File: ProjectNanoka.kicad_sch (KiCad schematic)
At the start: 32 parts, among them K1 2-1462038-1, P1 ST_20A, Q1 2SC1815, Q2 2SC1815, U1 TLV70033DDCR, U2 NC7WZ16P6X, U3 PS1440P02BT

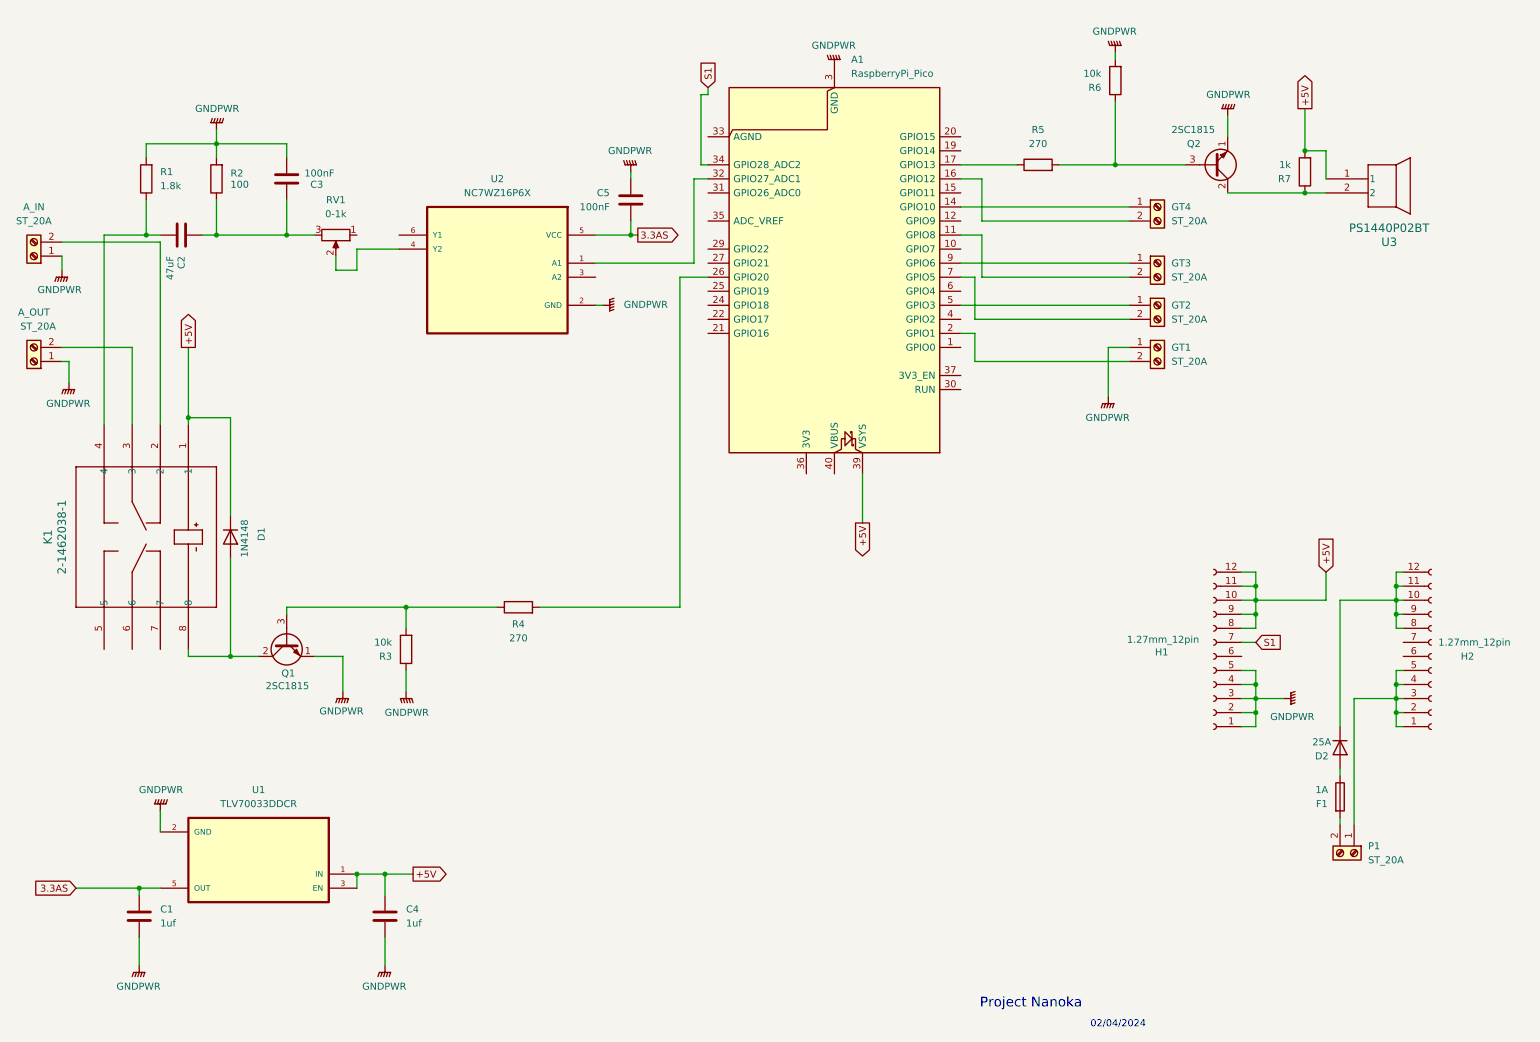
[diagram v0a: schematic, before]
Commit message: Fix issues found in v1
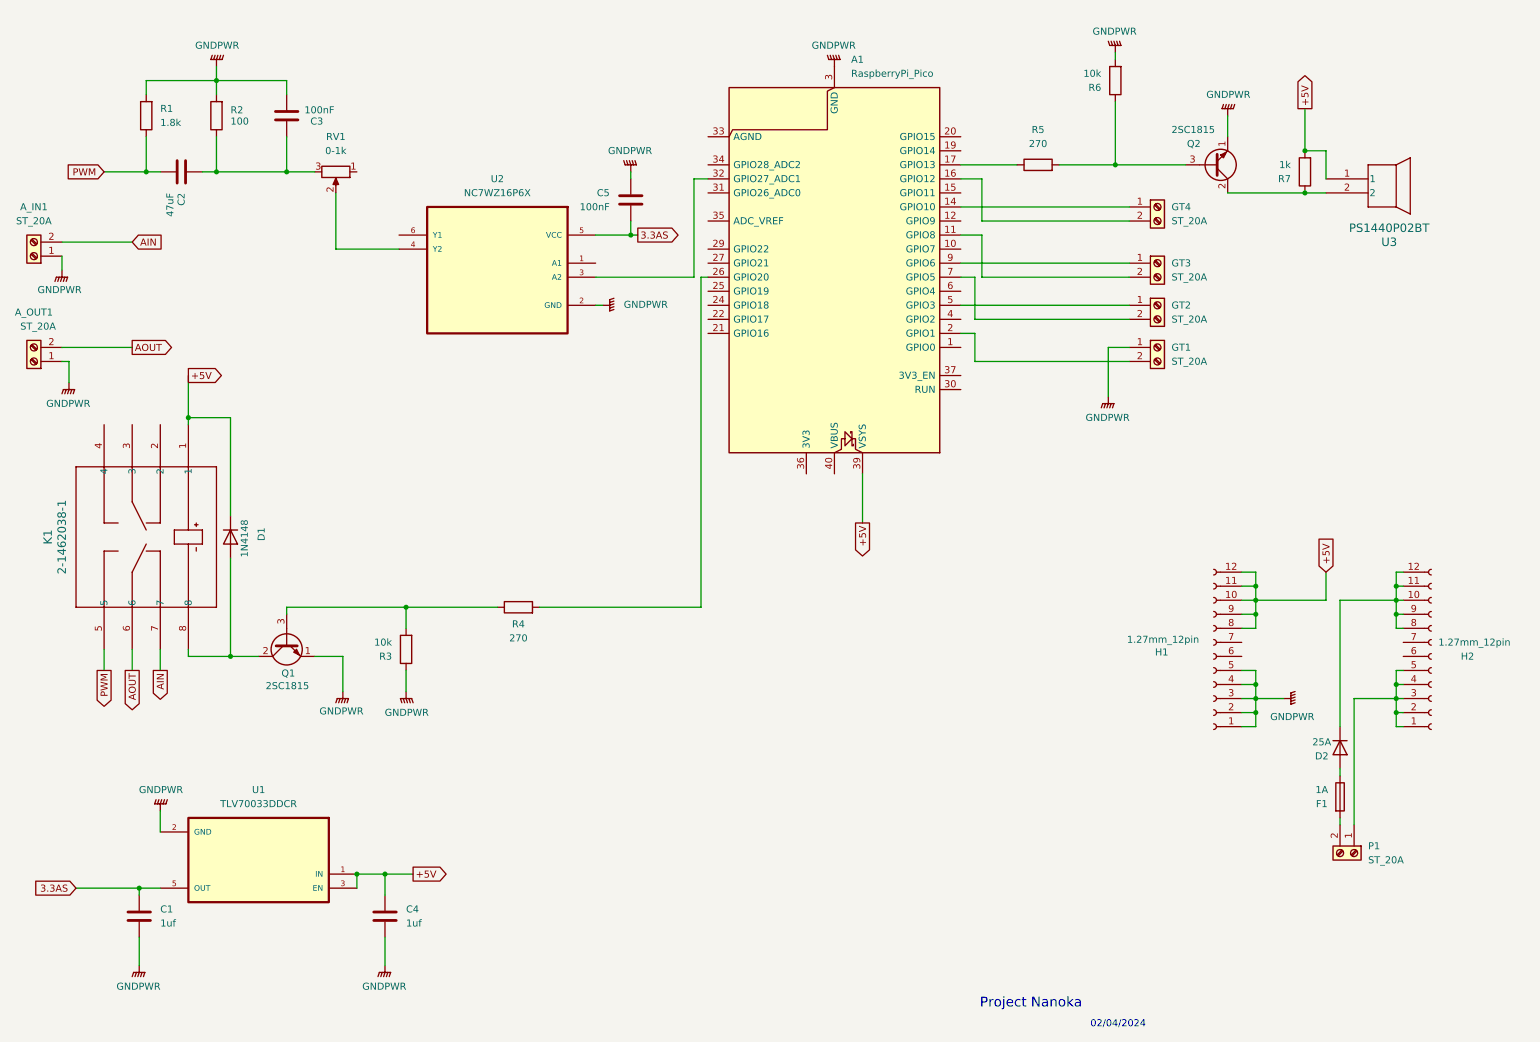
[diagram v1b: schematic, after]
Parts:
- K1: footprint Custom:RELAY8_THTNRW_TEC -> Custom:RELAY8-TH_NON-LATCH_1-COIL
- renumbered A_IN to A_IN1, A_OUT to A_OUT1
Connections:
- net at K1.3: no longer A_OUT1.2 (Pin_2)
- net PWM: now reaches C2.2, R1.1
- net PWM: now also K1.5; no longer K1.4
- net at A1.32 (GPIO27_ADC1): now also U2.3 (A2); no longer U2.1 (A1)
- net at K1.2: no longer A_IN1.2 (Pin_2)
- net AOUT: now reaches K1.6
- net AOUT: now also A_OUT1.2 (Pin_2)
- net AIN: now reaches K1.7
- net AIN: now also A_IN1.2 (Pin_2)
- net S1: no longer names the net of H1.7 (Pin_7)
- net S1: no longer A1.34 (GPIO28_ADC2)
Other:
- moved on the sheet: C2, C3, R1, R2, RV1

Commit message: Make improvements to board
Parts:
- A1: footprint Custom:RPi_Pico_SMD_TH -> Footprints:RPi_Pico_SMD_TH; symbol MCU_Module:RaspberryPi_Pico -> Symbols:RaspberryPi_Pico
- A_IN1, A_OUT1, GT1, GT2, GT3, GT4, P1: footprint Custom:CONN_1935161_PXC -> Footprints:CONN_1935161_PXC; symbol Connector:Screw_Terminal_01x02 -> Symbols:Screw_Terminal_01x02
- C1, C4: footprint Custom:CAP_C330C_MR_X7R_KEM -> Footprints:CAP_C330C_MR_X7R_KEM; symbol Device:C -> Symbols:C
- C2: footprint Custom:CAP_UUQ_5X5P4_NCH -> Footprints:CAP_UUQ_5X5P4_NCH; symbol Device:C -> Symbols:C
- C3, C5: footprint Custom:CAP_C320_KEM -> Footprints:CAP_C320_KEM; symbol Device:C -> Symbols:C
- D1: footprint Diode_THT:D_DO-35_SOD27_P7.62mm_Horizontal -> Footprints:D_DO-35_SOD27_P7.62mm_Horizontal; symbol Diode:1N4148 -> Symbols:1N4148
- D2: footprint Custom:P33_D5.4x7.5 -> Footprints:P33_D5.4x7.5; symbol Device:D -> Symbols:D
- F1: footprint Custom:20x300_FUSE_HOLDER_0PTF0078P_LTF -> Footprints:20x300_FUSE_HOLDER_0PTF0078P_LTF; symbol Device:Fuse -> Symbols:Fuse
- H1, H2: footprint Custom:PinHeader_1x12_P1.27mm_Vertical_Modded -> Footprints:PinHeader_1x12_P1.27mm_Vertical_Modded; symbol Connector:Conn_01x12_Socket -> Symbols:Conn_01x12_Socket
- K1: footprint Custom:RELAY8-TH_NON-LATCH_1-COIL -> Footprints:RELAY8-TH_NON-LATCH_1-COIL; symbol audio relay 2:2-1462038-1 -> Symbols:2-1462038-1
- Q1, Q2: footprint Package_TO_SOT_THT:TO-92_Inline -> Footprints:TO-92_Inline; symbol Transistor_BJT:2SC1815 -> Symbols:2SC1815
- R1, R2: footprint Custom:STA_CF14_STP -> Footprints:STA_CF14_STP; symbol Device:R -> Symbols:R
- R3, R4, R5, R6, R7: footprint Custom:STA_RNF14_STP -> Footprints:STA_RNF14_STP; symbol Device:R -> Symbols:R
- RV1: footprint Custom:TRIM_3310Y-101-102L -> Footprints:TRIM_3310Y-101-102L; symbol Device:R_Potentiometer -> Symbols:R_Potentiometer
- U1: footprint Custom:SOT95P280X110-5N -> Footprints:SOT95P280X110-5N; symbol TLV70033DDCR:TLV70033DDCR -> Symbols:TLV70033DDCR
- U2: footprint Custom:SOT65P210X110-6N -> Footprints:SOT65P210X110-6N; symbol NC7WZ16P6X:NC7WZ16P6X -> Symbols:NC7WZ16P6X
- U3: footprint Custom:PS1440P02BT_TDK -> Footprints:PS1440P02BT_TDK; symbol piezo:PS1440P02BT -> Symbols:PS1440P02BT

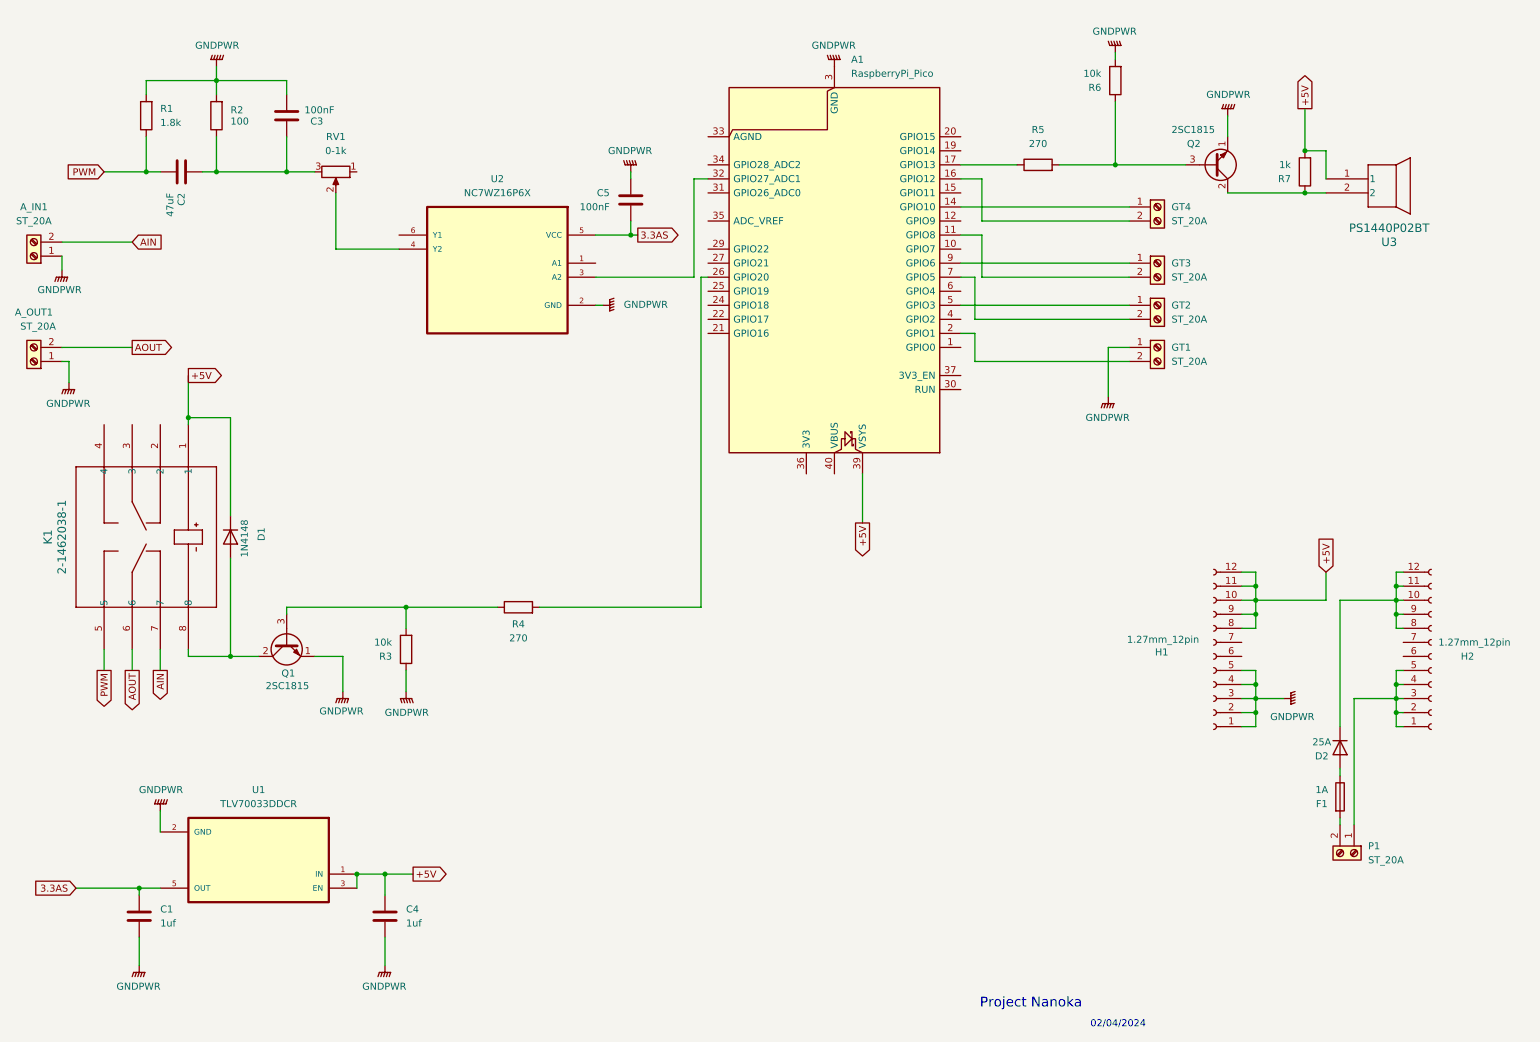
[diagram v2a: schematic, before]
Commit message: Replaced 2SC1815 with 2N3904BU
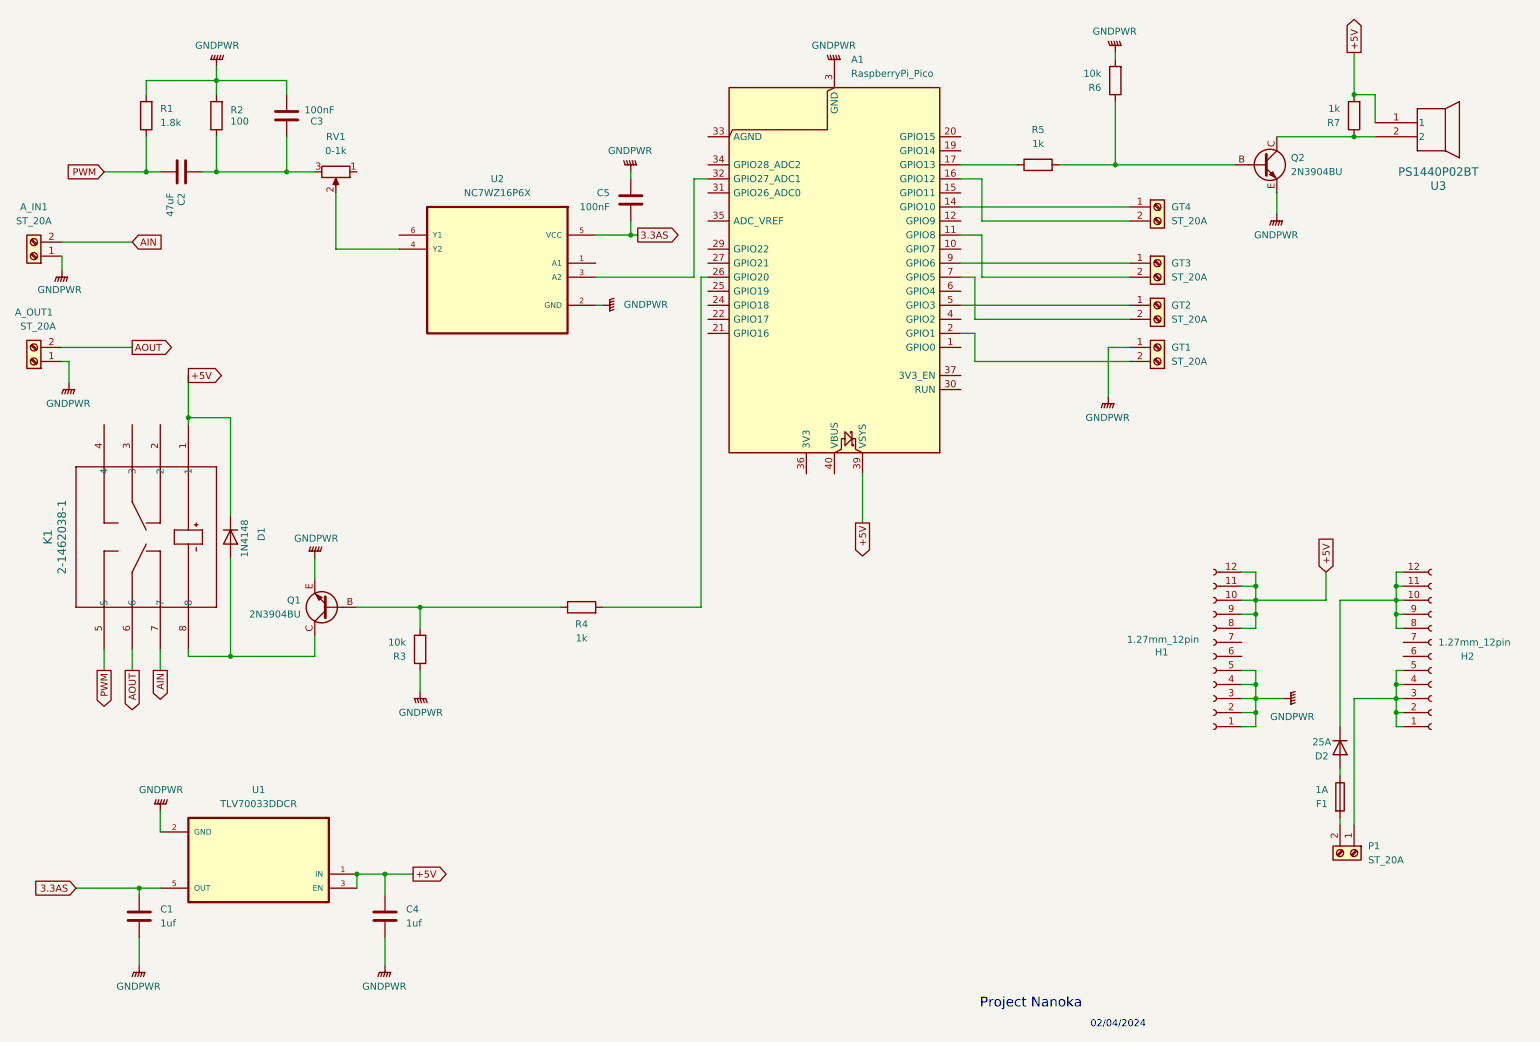
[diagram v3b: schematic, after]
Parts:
- removed Q1, Q2: 2SC1815, Footprints:TO-92_Inline, symbol Symbols:2SC1815
- added Q1, Q2: 2N3904BU, Footprints:2N3904BU, symbol Symbols:2N3904BU
- R4, R5: value 270 -> 1k
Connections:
- net GNDPWR: now also Q1.E, Q2.E
- net at R5.2, R6.1: now also Q2.B
- net at R7.1, U3.2: now also Q2.C
- net at R3.2, R4.1: now also Q1.B
- net at D1.2 (A), K1.8: now also Q1.C
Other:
- moved on the sheet: R3, R4, R7, U3

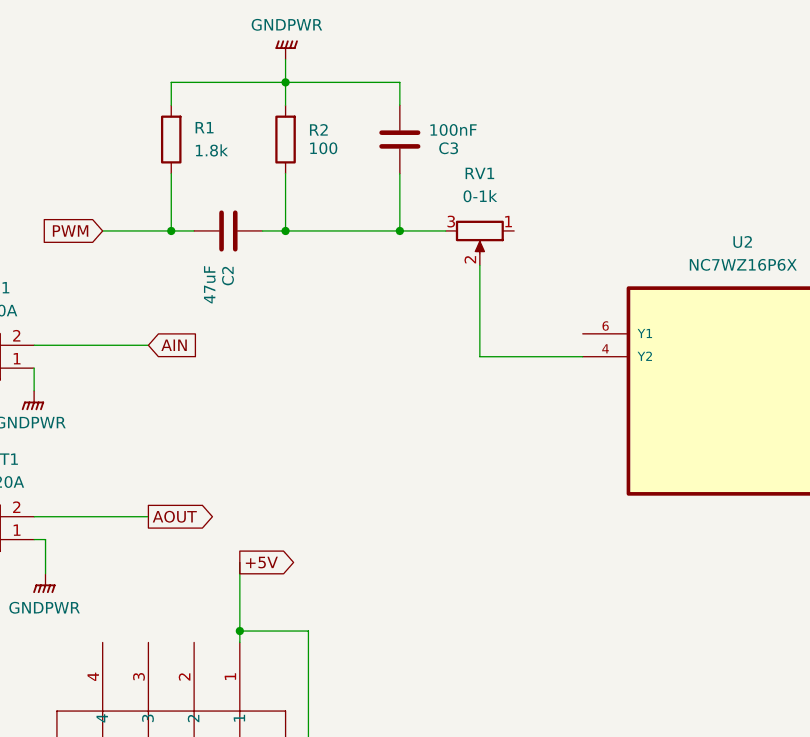
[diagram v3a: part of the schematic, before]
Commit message: Replaced RV1 with a 220ohm resistor
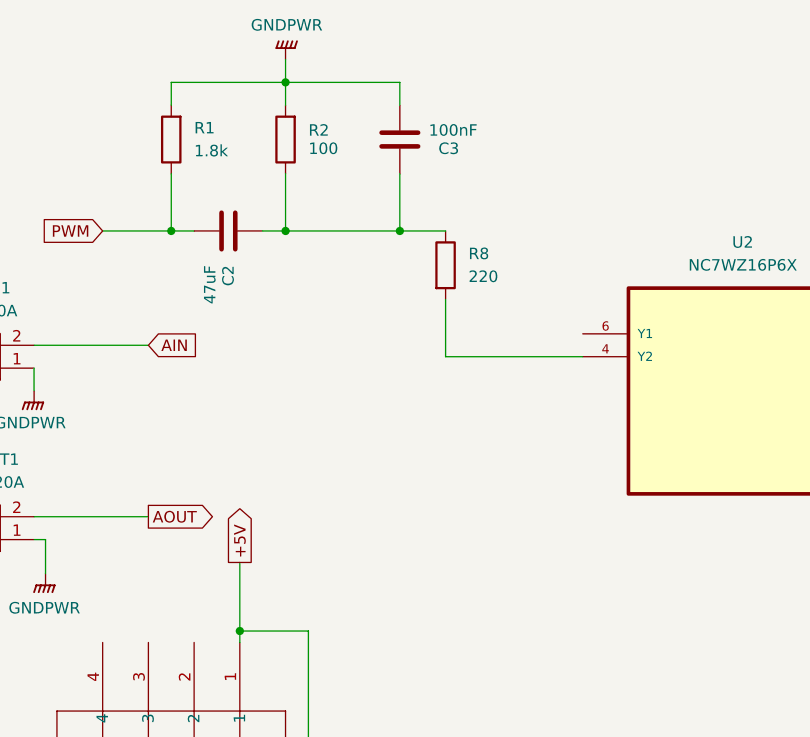
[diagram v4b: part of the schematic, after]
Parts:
- removed RV1: 0-1k, Footprints:TRIM_3310Y-101-102L, symbol Symbols:R_Potentiometer
- added R8: 220, Footprints:STA_RNMF14_STP, symbol Symbols:R
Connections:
- net at U2.4 (Y2): now also R8.2
- net at C2.1, C3.1, R2.1: now also R8.1
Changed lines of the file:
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@@
 	(wire
 		(pts
-			(xy 71.12 53.34) (xy 82.55 53.34)
+			(xy 67.31 53.34) (xy 82.55 53.34)
 		)
 		(stroke
@@
 	(wire
 		(pts
-			(xy 71.12 43.18) (xy 71.12 53.34)
+			(xy 67.31 46.99) (xy 67.31 53.34)
 		)
 		(stroke
@@
 	(global_label "+5V"
 		(shape output)
-		(at 44.45 76.2 0)
+		(at 44.45 76.2 90)
 		(fields_autoplaced yes)
 		(effects
@@
 		)
 		(property "Intersheetrefs" "${INTERSHEET_REFS}"
-			(at 51.3057 76.2 0)
+			(at 44.45 69.3443 90)
 			(effects
 				(font
@@
 				(path "/b82cdc01-ed0f-4544-82ee-3986c13336e7"
 					(reference "#PWR03")
-					(unit 1)
-				)
-			)
-		)
-	)
-	(symbol
-		(lib_id "Symbols:R_Potentiometer")
-		(at 71.12 39.37 270)
-		(unit 1)
-		(exclude_from_sim no)
-		(in_bom yes)
-		(on_board yes)
-		(dnp no)
-		(property "Reference" "RV1"
-			(at 71.12 33.02 90)
-			(effects
-				(font
-					(size 1.27 1.27)
-				)
-			)
-		)
-		(property "Value" "0-1k"
-			(at 71.12 35.56 90)
-			(effects
-				(font
-					(size 1.27 1.27)
-				)
-			)
-		)
-		(property "Footprint" "Footprints:TRIM_3310Y-101-102L"
-			(at 71.12 39.37 0)
-			(effects
-				(font
-					(size 1.27 1.27)
-				)
-				(hide yes)
-			)
-		)
-		(property "Datasheet" "~"
-			(at 71.12 39.37 0)
-			(effects
-				(font
-					(size 1.27 1.27)
-				)
-				(hide yes)
-			)
-		)
-		(property "Description" "Potentiometer"
-			(at 71.12 39.37 0)
-			(effects
-				(font
-					(size 1.27 1.27)
-				)
-				(hide yes)
-			)
-		)
-		(pin "1"
-		)
-		(pin "2"
-		)
-		(pin "3"
-		)
-		(instances
-			(project ""
-				(path "/b82cdc01-ed0f-4544-82ee-3986c13336e7"
-					(reference "RV1")
 					(unit 1)
 				)
@@
 					(unit 1)
 				)
+			)
+		)
+	)
+	(symbol
+		(lib_id "Symbols:R")
+		(at 67.31 43.18 0)
+		(unit 1)
+		(exclude_from_sim no)
+		(in_bom yes)
+		(on_board yes)
+		(dnp no)
+		(fields_autoplaced yes)
+		(property "Reference" "R8"
+			(at 69.85 41.9099 0)
+			(effects
+				(font
+					(size 1.27 1.27)
+				)
+				(justify left)
+			)
+		)
+		(property "Value" "220"
+			(at 69.85 44.4499 0)
+			(effects
+				(font
+					(size 1.27 1.27)
+				)
+				(justify left)
+			)
+		)
+		(property "Footprint" "Footprints:STA_RNMF14_STP"
+			(at 65.532 43.18 90)
+			(effects
+				(font
+					(size 1.27 1.27)
+				)
+				(hide yes)
+			)
+		)
+		(property "Datasheet" "~"
+			(at 67.31 43.18 0)
+			(effects
+				(font
+					(size 1.27 1.27)
+				)
+				(hide yes)
+			)
+		)
+		(property "Description" "Resistor"
+			(at 67.31 43.18 0)
+			(effects
+				(font
+					(size 1.27 1.27)
+				)
+				(hide yes)
+			)
+		)
+		(pin "2"
+		)
+		(pin "1"
+		)
+		(instances
+			(project ""
+				(path "/b82cdc01-ed0f-4544-82ee-3986c13336e7"
+					(reference "R8")
+					(unit 1)
+				)
